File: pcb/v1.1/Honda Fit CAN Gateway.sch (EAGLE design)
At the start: 19 parts, among them Q1 10MHz, U1 TEENSY_3.1_BASIC, U2 MCP2515TSOP, U3 TJA1050, U4 TJA1050, X1 CON_10X2F_JAE_MX34020NF1

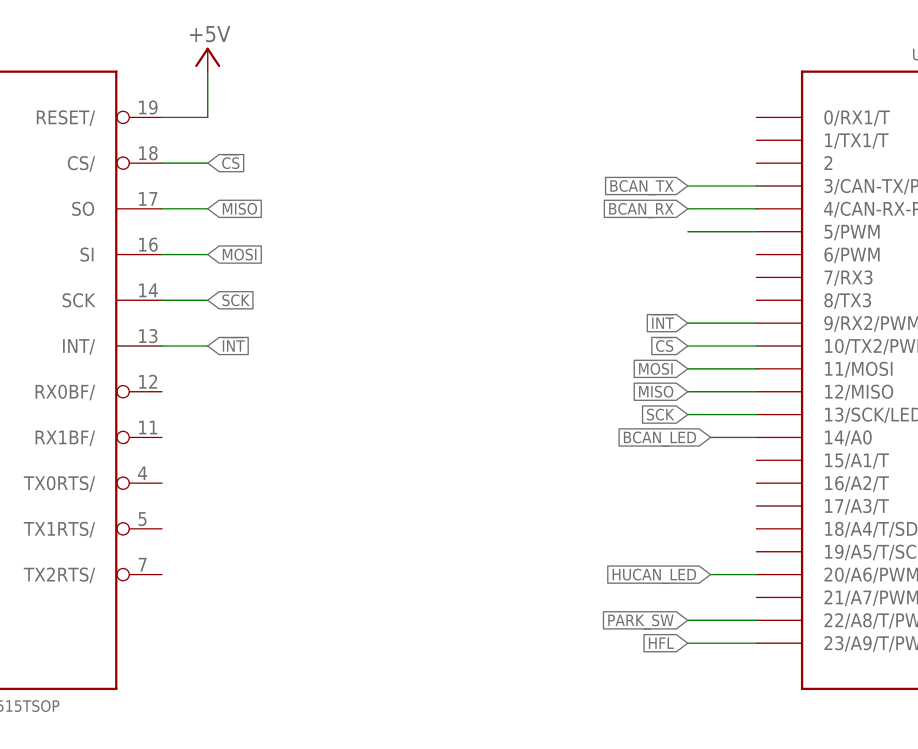
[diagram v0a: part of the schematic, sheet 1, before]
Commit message: Add series resistors on MCP2515 SPI lines
Lands can be used for any 0603 part
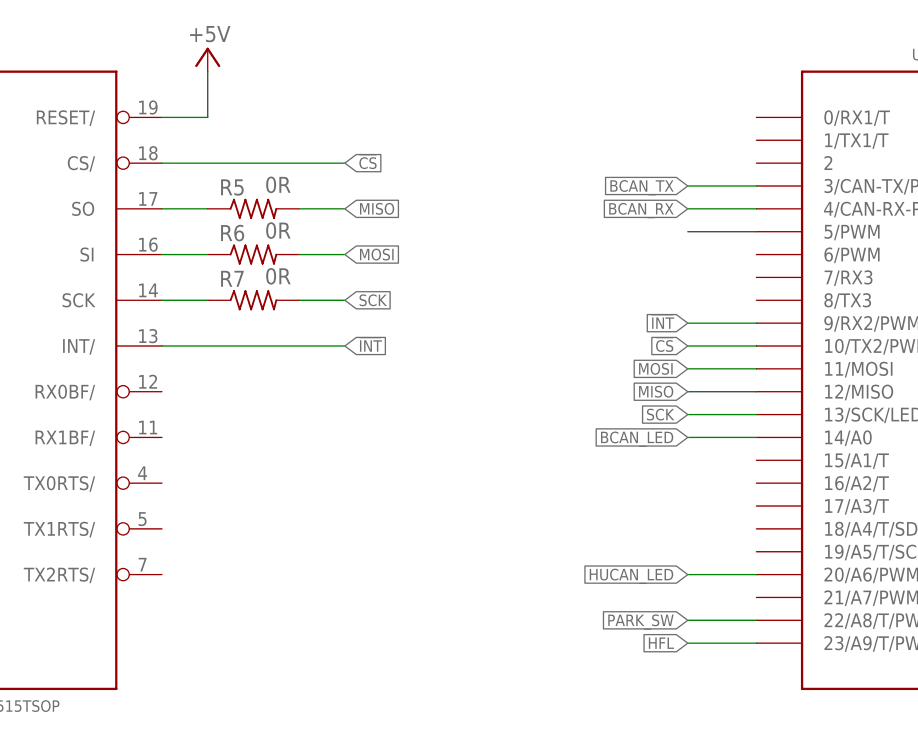
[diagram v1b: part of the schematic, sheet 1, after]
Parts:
- added R5, R6, R7: 0R, resistor:R-US_R0805
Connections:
- new net N$6: R5.1, U2.SO
- new net N$7: R6.1, U2.SI
- new net N$8: R7.1, U2.SCK
- net MISO: now also R5.2; no longer U2.SO
- net MOSI: now also R6.2; no longer U2.SI
- net SCK: now also R7.2; no longer U2.SCK
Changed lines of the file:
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@@
 <part name="SUPPLY3" library="supply2" deviceset="GND" device=""/>
 <part name="R4" library="resistor" deviceset="R-US_" device="R0805" value="120R"/>
+<part name="R5" library="resistor" deviceset="R-US_" device="R0805" value="0R"/>
+<part name="R6" library="resistor" deviceset="R-US_" device="R0805" value="0R"/>
+<part name="R7" library="resistor" deviceset="R-US_" device="R0805" value="0R"/>
 </parts>
 <sheets>
@@
 <instance part="D2" gate="G$1" x="175.26" y="83.82" rot="R90"/>
 <instance part="SUPPLY3" gate="GND" x="170.18" y="76.2"/>
+<instance part="R5" gate="G$1" x="111.76" y="162.56" smashed="yes">
+<attribute name="NAME" x="107.95" y="164.0586" size="1.778" layer="95"/>
+<attribute name="VALUE" x="113.03" y="164.338" size="1.778" layer="96"/>
+</instance>
+<instance part="R6" gate="G$1" x="111.76" y="157.48" smashed="yes">
+<attribute name="NAME" x="107.95" y="158.9786" size="1.778" layer="95"/>
+<attribute name="VALUE" x="113.03" y="159.258" size="1.778" layer="96"/>
+</instance>
+<instance part="R7" gate="G$1" x="111.76" y="152.4" smashed="yes">
+<attribute name="NAME" x="107.95" y="153.8986" size="1.778" layer="95"/>
+<attribute name="VALUE" x="113.03" y="154.178" size="1.778" layer="96"/>
+</instance>
 </instances>
 <busses>
@@
 <net name="SCK" class="0">
 <segment>
-<wire x1="106.68" y1="152.4" x2="101.6" y2="152.4" width="0.1524" layer="91"/>
-<pinref part="U2" gate="G$1" pin="SCK"/>
-<label x="106.68" y="152.4" size="1.27" layer="95" rot="MR180" xref="yes"/>
-</segment>
-<segment>
 <pinref part="U1" gate="G$1" pin="13/SCK/LED"/>
 <wire x1="167.64" y1="139.7" x2="160.02" y2="139.7" width="0.1524" layer="91"/>
 <label x="160.02" y="139.7" size="1.27" layer="95" rot="R180" xref="yes"/>
 </segment>
+<segment>
+<pinref part="R7" gate="G$1" pin="2"/>
+<wire x1="116.84" y1="152.4" x2="121.92" y2="152.4" width="0.1524" layer="91"/>
+<label x="121.92" y="152.4" size="1.27" layer="95" xref="yes"/>
+</segment>
 </net>
 <net name="MISO" class="0">
@@
 </segment>
 <segment>
-<wire x1="106.68" y1="162.56" x2="101.6" y2="162.56" width="0.1524" layer="91"/>
-<pinref part="U2" gate="G$1" pin="SO"/>
-<label x="106.68" y="162.56" size="1.27" layer="95" rot="MR180" xref="yes"/>
+<pinref part="R5" gate="G$1" pin="2"/>
+<wire x1="116.84" y1="162.56" x2="121.92" y2="162.56" width="0.1524" layer="91"/>
+<label x="121.92" y="162.56" size="1.27" layer="95" xref="yes"/>
 </segment>
 </net>
 <net name="MOSI" class="0">
-<segment>
-<wire x1="106.68" y1="157.48" x2="101.6" y2="157.48" width="0.1524" layer="91"/>
-<pinref part="U2" gate="G$1" pin="SI"/>
-<label x="106.68" y="157.48" size="1.27" layer="95" rot="MR180" xref="yes"/>
-</segment>
 <segment>
 <pinref part="U1" gate="G$1" pin="11/MOSI"/>
@@
 <label x="160.02" y="144.78" size="1.27" layer="95" rot="R180" xref="yes"/>
 </segment>
+<segment>
+<pinref part="R6" gate="G$1" pin="2"/>
+<wire x1="116.84" y1="157.48" x2="121.92" y2="157.48" width="0.1524" layer="91"/>
+<label x="121.92" y="157.48" size="1.27" layer="95" xref="yes"/>
+</segment>
 </net>
 <net name="BCAN_RX" class="0">
@@
 </segment>
 <segment>
-<wire x1="106.68" y1="167.64" x2="101.6" y2="167.64" width="0.1524" layer="91"/>
+<wire x1="121.92" y1="167.64" x2="101.6" y2="167.64" width="0.1524" layer="91"/>
 <pinref part="U2" gate="G$1" pin="CS/"/>
-<label x="106.68" y="167.64" size="1.27" layer="95" rot="MR180" xref="yes"/>
+<label x="121.92" y="167.64" size="1.27" layer="95" rot="MR180" xref="yes"/>
 </segment>
 </net>
 <net name="!INT" class="0">
 <segment>
-<wire x1="106.68" y1="147.32" x2="101.6" y2="147.32" width="0.1524" layer="91"/>
+<wire x1="121.92" y1="147.32" x2="101.6" y2="147.32" width="0.1524" layer="91"/>
 <pinref part="U2" gate="G$1" pin="INT/"/>
-<label x="106.68" y="147.32" size="1.27" layer="95" rot="MR180" xref="yes"/>
+<label x="121.92" y="147.32" size="1.27" layer="95" rot="MR180" xref="yes"/>
 </segment>
 <segment>
@@
 <segment>
 <pinref part="U1" gate="G$1" pin="20/A6/PWM"/>
-<wire x1="162.56" y1="121.92" x2="167.64" y2="121.92" width="0.1524" layer="91"/>
-<label x="162.56" y="121.92" size="1.27" layer="95" rot="R180" xref="yes"/>
+<wire x1="160.02" y1="121.92" x2="167.64" y2="121.92" width="0.1524" layer="91"/>
+<label x="160.02" y="121.92" size="1.27" layer="95" rot="R180" xref="yes"/>
 </segment>
 </net>
@@
 <segment>
 <pinref part="U1" gate="G$1" pin="14/A0"/>
-<wire x1="167.64" y1="137.16" x2="162.56" y2="137.16" width="0.1524" layer="91"/>
-<label x="162.56" y="137.16" size="1.27" layer="95" rot="R180" xref="yes"/>
-</segment>
-</net>
+<wire x1="167.64" y1="137.16" x2="160.02" y2="137.16" width="0.1524" layer="91"/>
+<label x="160.02" y="137.16" size="1.27" layer="95" rot="R180" xref="yes"/>
+</segment>
+</net>
+<net name="N$6" class="0">
+<segment>
+<pinref part="U2" gate="G$1" pin="SO"/>
+<pinref part="R5" gate="G$1" pin="1"/>
+<wire x1="101.6" y1="162.56" x2="106.68" y2="162.56" width="0.1524" layer="91"/>
+</segment>
+</net>
+<net name="N$7" class="0">
+<segment>
+<pinref part="U2" gate="G$1" pin="SI"/>
+<pinref part="R6" gate="G$1" pin="1"/>
+<wire x1="101.6" y1="157.48" x2="106.68" y2="157.48" width="0.1524" layer="91"/>
+</segment>
+</net>
+<net name="N$8" class="0">
+<segment>
+<pinref part="U2" gate="G$1" pin="SCK"/>
+<pinref part="R7" gate="G$1" pin="1"/>
+<wire x1="101.6" y1="152.4" x2="106.68" y2="152.4" width="0.1524" layer="91"/>
+</segment>
+</net>

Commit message: Add 10k pullup for reset
Datasheet recommended
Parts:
- added R8: 10k, resistor:R-US_R0805
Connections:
- new net N$9: R8.1, U2.RESET/
- net +5V: now also R8.2; no longer U2.RESET/
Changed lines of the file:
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@@
 <part name="R6" library="resistor" deviceset="R-US_" device="R0805" value="0R"/>
 <part name="R7" library="resistor" deviceset="R-US_" device="R0805" value="0R"/>
+<part name="R8" library="resistor" deviceset="R-US_" device="R0805" value="10k"/>
 </parts>
 <sheets>
@@
 <instance part="FRAME1" gate="G$1" x="0" y="0"/>
 <instance part="FRAME1" gate="G$2" x="172.72" y="0"/>
-<instance part="P+3" gate="1" x="106.68" y="180.34" smashed="yes">
-<attribute name="VALUE" x="109.22" y="182.88" size="1.778" layer="96" rot="R180"/>
+<instance part="P+3" gate="1" x="109.22" y="190.5" smashed="yes">
+<attribute name="VALUE" x="111.76" y="193.04" size="1.778" layer="96" rot="R180"/>
 </instance>
 <instance part="R2" gate="G$1" x="187.96" y="91.44"/>
@@
 <attribute name="NAME" x="107.95" y="153.8986" size="1.778" layer="95"/>
 <attribute name="VALUE" x="113.03" y="154.178" size="1.778" layer="96"/>
+</instance>
+<instance part="R8" gate="G$1" x="109.22" y="180.34" smashed="yes" rot="R90">
+<attribute name="NAME" x="107.7214" y="176.53" size="1.778" layer="95" rot="R90"/>
+<attribute name="VALUE" x="107.442" y="181.61" size="1.778" layer="96" rot="R90"/>
 </instance>
 </instances>
@@
 </segment>
 <segment>
-<pinref part="U2" gate="G$1" pin="RESET/"/>
+<pinref part="R8" gate="G$1" pin="2"/>
 <pinref part="P+3" gate="1" pin="+5V"/>
-<wire x1="101.6" y1="172.72" x2="106.68" y2="172.72" width="0.1524" layer="91"/>
-<wire x1="106.68" y1="172.72" x2="106.68" y2="177.8" width="0.1524" layer="91"/>
+<wire x1="109.22" y1="187.96" x2="109.22" y2="185.42" width="0.1524" layer="91"/>
 </segment>
 </net>
@@
 </segment>
 </net>
+<net name="N$9" class="0">
+<segment>
+<pinref part="U2" gate="G$1" pin="RESET/"/>
+<wire x1="101.6" y1="172.72" x2="109.22" y2="172.72" width="0.1524" layer="91"/>
+<pinref part="R8" gate="G$1" pin="1"/>
+<wire x1="109.22" y1="172.72" x2="109.22" y2="175.26" width="0.1524" layer="91"/>
+</segment>
+</net>

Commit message: Replace xtal with oscillator.  Connect reset to Teensy
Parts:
- removed C2: (no value), resistor:C-EUC0603
- removed Q1: 10MHz, crystal:CRYSTALHC49S
- added R9: 10k, resistor:R-US_R0805
- added U5: CB3, ductapemaster_custom:CB3
- C1: value (none) -> 100n
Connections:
- removed net N$2: C2.1, Q1.1, U2.OSC1
- removed net N$3: U1.5/PWM
- removed net N$9: R8.1, U2.RESET/
- new net !RESET: R8.1, U1.5/PWM, U2.RESET/
- new net CLK_10MHZ: U2.OSC1, U5.XO
- net +5V: now also C1.1, U5.EN, U5.VCC
- net GND: now also R9.1, U5.GND; no longer C2.2
- net N$1: now also R9.2; no longer C1.1, Q1.2
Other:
- moved on the sheet: C1
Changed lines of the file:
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@@
 <part name="P+4" library="supply1" deviceset="+5V" device=""/>
 <part name="SUPPLY4" library="supply2" deviceset="GND" device=""/>
-<part name="Q1" library="crystal" deviceset="CRYSTAL" device="HC49S" value="10MHz"/>
-<part name="C1" library="resistor" deviceset="C-EU" device="C0603"/>
-<part name="C2" library="resistor" deviceset="C-EU" device="C0603"/>
 <part name="SUPPLY5" library="supply2" deviceset="GND" device=""/>
 <part name="C3" library="resistor" deviceset="C-EU" device="C0603" value="100n"/>
@@
 <part name="R7" library="resistor" deviceset="R-US_" device="R0805" value="0R"/>
 <part name="R8" library="resistor" deviceset="R-US_" device="R0805" value="10k"/>
+<part name="R9" library="resistor" deviceset="R-US_" device="R0805" value="10k"/>
+<part name="U5" library="ductapemaster_custom" deviceset="CB3" device=""/>
+<part name="P+6" library="supply1" deviceset="+5V" device=""/>
+<part name="C1" library="resistor" deviceset="C-EU" device="C0603" value="100n"/>
+<part name="SUPPLY7" library="supply2" deviceset="GND" device=""/>
 </parts>
 <sheets>
@@
 </instance>
 <instance part="SUPPLY4" gate="GND" x="53.34" y="127"/>
-<instance part="Q1" gate="G$1" x="48.26" y="111.76" smashed="yes" rot="R180">
-<attribute name="NAME" x="53.34" y="115.824" size="1.778" layer="95" rot="R180"/>
-<attribute name="VALUE" x="45.72" y="114.3" size="1.778" layer="96" rot="R180"/>
-</instance>
-<instance part="C1" gate="G$1" x="43.18" y="106.68"/>
-<instance part="C2" gate="G$1" x="53.34" y="106.68"/>
-<instance part="SUPPLY5" gate="GND" x="48.26" y="93.98"/>
+<instance part="SUPPLY5" gate="GND" x="40.64" y="109.22"/>
 <instance part="C3" gate="G$1" x="53.34" y="139.7" rot="MR0"/>
 <instance part="FRAME1" gate="G$1" x="0" y="0"/>
@@
 <attribute name="VALUE" x="107.442" y="181.61" size="1.778" layer="96" rot="R90"/>
 </instance>
+<instance part="R9" gate="G$1" x="53.34" y="116.84" smashed="yes">
+<attribute name="NAME" x="49.53" y="118.3386" size="1.778" layer="95"/>
+<attribute name="VALUE" x="54.61" y="118.618" size="1.778" layer="96"/>
+</instance>
+<instance part="U5" gate="G$1" x="81.28" y="83.82"/>
+<instance part="P+6" gate="1" x="66.04" y="101.6" smashed="yes">
+<attribute name="VALUE" x="68.58" y="104.14" size="1.778" layer="96" rot="R180"/>
+</instance>
+<instance part="C1" gate="G$1" x="66.04" y="86.36" rot="MR0"/>
+<instance part="SUPPLY7" gate="GND" x="66.04" y="71.12"/>
 </instances>
 <busses>
@@
 </segment>
 <segment>
-<pinref part="C1" gate="G$1" pin="2"/>
 <pinref part="SUPPLY5" gate="GND" pin="GND"/>
-<wire x1="43.18" y1="101.6" x2="43.18" y2="99.06" width="0.1524" layer="91"/>
-<wire x1="43.18" y1="99.06" x2="48.26" y2="99.06" width="0.1524" layer="91"/>
-<pinref part="C2" gate="G$1" pin="2"/>
-<wire x1="48.26" y1="99.06" x2="48.26" y2="96.52" width="0.1524" layer="91"/>
-<wire x1="48.26" y1="99.06" x2="53.34" y2="99.06" width="0.1524" layer="91"/>
-<wire x1="53.34" y1="99.06" x2="53.34" y2="101.6" width="0.1524" layer="91"/>
-<junction x="48.26" y="99.06"/>
+<wire x1="40.64" y1="116.84" x2="40.64" y2="111.76" width="0.1524" layer="91"/>
+<pinref part="R9" gate="G$1" pin="1"/>
+<wire x1="40.64" y1="116.84" x2="48.26" y2="116.84" width="0.1524" layer="91"/>
 </segment>
 <segment>
@@
 <junction x="170.18" y="83.82"/>
 <pinref part="SUPPLY3" gate="GND" pin="GND"/>
+</segment>
+<segment>
+<pinref part="C1" gate="G$1" pin="2"/>
+<pinref part="SUPPLY7" gate="GND" pin="GND"/>
+<wire x1="66.04" y1="81.28" x2="66.04" y2="76.2" width="0.1524" layer="91"/>
+<pinref part="U5" gate="G$1" pin="GND"/>
+<wire x1="66.04" y1="76.2" x2="66.04" y2="73.66" width="0.1524" layer="91"/>
+<wire x1="66.04" y1="76.2" x2="68.58" y2="76.2" width="0.1524" layer="91"/>
+<junction x="66.04" y="76.2"/>
 </segment>
 </net>
@@
 <wire x1="109.22" y1="187.96" x2="109.22" y2="185.42" width="0.1524" layer="91"/>
 </segment>
+<segment>
+<pinref part="C1" gate="G$1" pin="1"/>
+<pinref part="P+6" gate="1" pin="+5V"/>
+<wire x1="66.04" y1="88.9" x2="66.04" y2="91.44" width="0.1524" layer="91"/>
+<pinref part="U5" gate="G$1" pin="VCC"/>
+<wire x1="66.04" y1="91.44" x2="66.04" y2="96.52" width="0.1524" layer="91"/>
+<wire x1="66.04" y1="96.52" x2="66.04" y2="99.06" width="0.1524" layer="91"/>
+<wire x1="66.04" y1="91.44" x2="68.58" y2="91.44" width="0.1524" layer="91"/>
+<pinref part="U5" gate="G$1" pin="EN"/>
+<wire x1="93.98" y1="91.44" x2="96.52" y2="91.44" width="0.1524" layer="91"/>
+<wire x1="96.52" y1="91.44" x2="96.52" y2="96.52" width="0.1524" layer="91"/>
+<wire x1="96.52" y1="96.52" x2="66.04" y2="96.52" width="0.1524" layer="91"/>
+<junction x="66.04" y="96.52"/>
+<junction x="66.04" y="91.44"/>
+</segment>
 </net>
 <net name="HUCAN_RX" class="0">
@@
 </segment>
 </net>
-<net name="N$1" class="0">
-<segment>
-<pinref part="U2" gate="G$1" pin="OSC2"/>
-<pinref part="C1" gate="G$1" pin="1"/>
-<wire x1="63.5" y1="116.84" x2="43.18" y2="116.84" width="0.1524" layer="91"/>
-<wire x1="43.18" y1="116.84" x2="43.18" y2="111.76" width="0.1524" layer="91"/>
-<pinref part="Q1" gate="G$1" pin="2"/>
-<wire x1="43.18" y1="111.76" x2="43.18" y2="109.22" width="0.1524" layer="91"/>
-<wire x1="43.18" y1="111.76" x2="45.72" y2="111.76" width="0.1524" layer="91"/>
-<junction x="43.18" y="111.76"/>
-</segment>
-</net>
-<net name="N$2" class="0">
-<segment>
-<pinref part="U2" gate="G$1" pin="OSC1"/>
-<pinref part="C2" gate="G$1" pin="1"/>
-<wire x1="63.5" y1="111.76" x2="53.34" y2="111.76" width="0.1524" layer="91"/>
-<wire x1="53.34" y1="111.76" x2="53.34" y2="109.22" width="0.1524" layer="91"/>
-<pinref part="Q1" gate="G$1" pin="1"/>
-<wire x1="50.8" y1="111.76" x2="53.34" y2="111.76" width="0.1524" layer="91"/>
-<junction x="53.34" y="111.76"/>
-</segment>
-</net>
-<net name="N$3" class="0">
-<segment>
-<pinref part="U1" gate="G$1" pin="5/PWM"/>
-<wire x1="167.64" y1="160.02" x2="160.02" y2="160.02" width="0.1524" layer="91"/>
-</segment>
-</net>
 <net name="PARK_SW" class="0">
 <segment>
@@
 </segment>
 </net>
-<net name="N$9" class="0">
+<net name="!RESET" class="0">
 <segment>
 <pinref part="U2" gate="G$1" pin="RESET/"/>
@@
 <pinref part="R8" gate="G$1" pin="1"/>
 <wire x1="109.22" y1="172.72" x2="109.22" y2="175.26" width="0.1524" layer="91"/>
-</segment>
-</net>
+<wire x1="109.22" y1="172.72" x2="121.92" y2="172.72" width="0.1524" layer="91"/>
+<junction x="109.22" y="172.72"/>
+<label x="121.92" y="172.72" size="1.27" layer="95" xref="yes"/>
+</segment>
+<segment>
+<pinref part="U1" gate="G$1" pin="5/PWM"/>
+<wire x1="167.64" y1="160.02" x2="160.02" y2="160.02" width="0.1524" layer="91"/>
+<label x="160.02" y="160.02" size="1.27" layer="95" rot="R180" xref="yes"/>
+</segment>
+</net>
+<net name="N$1" class="0">
+<segment>
+<pinref part="U2" gate="G$1" pin="OSC2"/>
+<pinref part="R9" gate="G$1" pin="2"/>
+<wire x1="58.42" y1="116.84" x2="63.5" y2="116.84" width="0.1524" layer="91"/>
+</segment>
+</net>
+<net name="CLK_10MHZ" class="0">
+<segment>
+<pinref part="U2" gate="G$1" pin="OSC1"/>
+<wire x1="63.5" y1="111.76" x2="58.42" y2="111.76" width="0.1524" layer="91"/>
+<label x="58.42" y="111.76" size="1.27" layer="95" rot="R180" xref="yes"/>
+</segment>
+<segment>
+<pinref part="U5" gate="G$1" pin="XO"/>
+<wire x1="93.98" y1="76.2" x2="96.52" y2="76.2" width="0.1524" layer="91"/>
+<label x="96.52" y="76.2" size="1.27" layer="95" xref="yes"/>
+</segment>
+</net>
